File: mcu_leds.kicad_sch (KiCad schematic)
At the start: 8 parts, among them U1201 SN74LVC1G07DCKR

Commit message: Finish transitioning to RP2040
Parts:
- renumbered C1202 to C3901, D1203 to D3901, D1204 to D3902, D1205 to D3903, R1203 to R3901, R1206 to R3902, R1209 to R3903, U1201 to U3901
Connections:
- net VCC is gone; now on net +3.3V: R3903.1
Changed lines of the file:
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@@
 		)
 	)
-	(hierarchical_label "VCC"
-		(shape input)
-		(at 168.91 80.01 90)
-		(effects
-			(font
-				(size 1.27 1.27)
-			)
-			(justify left)
+	(symbol
+		(lib_id "power:+3.3V")
+		(at 168.91 80.01 0)
+		(unit 1)
+		(exclude_from_sim no)
+		(in_bom yes)
+		(on_board yes)
+		(dnp no)
+		(fields_autoplaced yes)
+		(property "Reference" "#PWR03907"
+			(at 168.91 83.82 0)
+			(effects
+				(font
+					(size 1.27 1.27)
+				)
+				(hide yes)
+			)
+		)
+		(property "Value" "+3.3V"
+			(at 171.45 78.7399 0)
+			(effects
+				(font
+					(size 1.27 1.27)
+				)
+				(justify left)
+			)
+		)
+		(property "Footprint" ""
+			(at 168.91 80.01 0)
+			(effects
+				(font
+					(size 1.27 1.27)
+				)
+				(hide yes)
+			)
+		)
+		(property "Datasheet" ""
+			(at 168.91 80.01 0)
+			(effects
+				(font
+					(size 1.27 1.27)
+				)
+				(hide yes)
+			)
+		)
+		(property "Description" "Power symbol creates a global label with name \"+3.3V\""
+			(at 168.91 80.01 0)
+			(effects
+				(font
+					(size 1.27 1.27)
+				)
+				(hide yes)
+			)
+		)
+		(pin "1"
+		)
+		(instances
+			(project "HALPI2"
+				(path "/abc482bd-3f17-4d35-80db-1da3dcdb5c27/850df4bf-e40a-4082-adc2-76804638b949/91cc707d-e26c-4ece-92aa-858b9215776e"
+					(reference "#PWR03907")
+					(unit 1)
+				)
+			)
 		)
 	)
@@
 		(on_board yes)
 		(dnp no)
-		(property "Reference" "R1209"
+		(property "Reference" "R3903"
 			(at 170.688 82.6516 0)
 			(effects
@@
 			(project "HALPI2"
 				(path "/abc482bd-3f17-4d35-80db-1da3dcdb5c27/850df4bf-e40a-4082-adc2-76804638b949/91cc707d-e26c-4ece-92aa-858b9215776e"
-					(reference "R1209")
+					(reference "R3903")
 					(unit 1)
 				)
@@
 		(dnp no)
 		(fields_autoplaced yes)
-		(property "Reference" "D1204"
+		(property "Reference" "D3902"
 			(at 156.21 91.7574 90)
 			(effects
@@
 			(project "HALPI2"
 				(path "/abc482bd-3f17-4d35-80db-1da3dcdb5c27/850df4bf-e40a-4082-adc2-76804638b949/91cc707d-e26c-4ece-92aa-858b9215776e"
-					(reference "D1204")
+					(reference "D3902")
 					(unit 1)
 				)
@@
 		(on_board yes)
 		(dnp no)
-		(property "Reference" "#PWR03817"
+		(property "Reference" "#PWR03901"
 			(at 106.68 90.17 0)
 			(effects
@@
 			(project "HALPI2"
 				(path "/abc482bd-3f17-4d35-80db-1da3dcdb5c27/850df4bf-e40a-4082-adc2-76804638b949/91cc707d-e26c-4ece-92aa-858b9215776e"
-					(reference "#PWR03817")
+					(reference "#PWR03901")
 					(unit 1)
 				)
@@
 		(on_board yes)
 		(dnp no)
-		(property "Reference" "D1205"
+		(property "Reference" "D3903"
 			(at 171.9072 90.4494 90)
 			(effects
@@
 			(project "HALPI2"
 				(path "/abc482bd-3f17-4d35-80db-1da3dcdb5c27/850df4bf-e40a-4082-adc2-76804638b949/91cc707d-e26c-4ece-92aa-858b9215776e"
-					(reference "D1205")
+					(reference "D3903")
 					(unit 1)
 				)
@@
 		(on_board yes)
 		(dnp no)
-		(property "Reference" "D1203"
+		(property "Reference" "D3901"
 			(at 141.4272 90.4494 90)
 			(effects
@@
 			(project "HALPI2"
 				(path "/abc482bd-3f17-4d35-80db-1da3dcdb5c27/850df4bf-e40a-4082-adc2-76804638b949/91cc707d-e26c-4ece-92aa-858b9215776e"
-					(reference "D1203")
+					(reference "D3901")
 					(unit 1)
 				)
@@
 		(dnp no)
 		(fields_autoplaced yes)
-		(property "Reference" "#PWR03820"
+		(property "Reference" "#PWR03904"
 			(at 138.43 83.82 0)
 			(effects
@@
 			(project "HALPI2"
 				(path "/abc482bd-3f17-4d35-80db-1da3dcdb5c27/850df4bf-e40a-4082-adc2-76804638b949/91cc707d-e26c-4ece-92aa-858b9215776e"
-					(reference "#PWR03820")
+					(reference "#PWR03904")
 					(unit 1)
 				)
@@
 		(on_board yes)
 		(dnp no)
-		(property "Reference" "U1201"
+		(property "Reference" "U3901"
 			(at 131.064 98.806 0)
 			(effects
@@
 			(project "HALPI2"
 				(path "/abc482bd-3f17-4d35-80db-1da3dcdb5c27/850df4bf-e40a-4082-adc2-76804638b949/91cc707d-e26c-4ece-92aa-858b9215776e"
-					(reference "U1201")
+					(reference "U3901")
 					(unit 1)
 				)
@@
 		(dnp no)
 		(fields_autoplaced yes)
-		(property "Reference" "#PWR03818"
+		(property "Reference" "#PWR03902"
 			(at 119.38 83.82 0)
 			(effects
@@
 			(project "HALPI2"
 				(path "/abc482bd-3f17-4d35-80db-1da3dcdb5c27/850df4bf-e40a-4082-adc2-76804638b949/91cc707d-e26c-4ece-92aa-858b9215776e"
-					(reference "#PWR03818")
+					(reference "#PWR03902")
 					(unit 1)
 				)
@@
 		(on_board yes)
 		(dnp no)
-		(property "Reference" "R1203"
+		(property "Reference" "R3901"
 			(at 140.208 82.6516 0)
 			(effects
@@
 			(project "HALPI2"
 				(path "/abc482bd-3f17-4d35-80db-1da3dcdb5c27/850df4bf-e40a-4082-adc2-76804638b949/91cc707d-e26c-4ece-92aa-858b9215776e"
-					(reference "R1203")
+					(reference "R3901")
 					(unit 1)
 				)
@@
 		(dnp no)
 		(fields_autoplaced yes)
-		(property "Reference" "#PWR03821"
+		(property "Reference" "#PWR03905"
 			(at 152.4 83.82 0)
 			(effects
@@
 			(project "HALPI2"
 				(path "/abc482bd-3f17-4d35-80db-1da3dcdb5c27/850df4bf-e40a-4082-adc2-76804638b949/91cc707d-e26c-4ece-92aa-858b9215776e"
-					(reference "#PWR03821")
+					(reference "#PWR03905")
 					(unit 1)
 				)
@@
 		(on_board yes)
 		(dnp no)
-		(property "Reference" "R1206"
+		(property "Reference" "R3902"
 			(at 154.178 82.6516 0)
 			(effects
@@
 			(project "HALPI2"
 				(path "/abc482bd-3f17-4d35-80db-1da3dcdb5c27/850df4bf-e40a-4082-adc2-76804638b949/91cc707d-e26c-4ece-92aa-858b9215776e"
-					(reference "R1206")
+					(reference "R3902")
 					(unit 1)
 				)
@@
 		(dnp no)
 		(fields_autoplaced yes)
-		(property "Reference" "C1202"
+		(property "Reference" "C3901"
 			(at 113.03 76.2 90)
 			(effects
@@
 			(project "HALPI2"
 				(path "/abc482bd-3f17-4d35-80db-1da3dcdb5c27/850df4bf-e40a-4082-adc2-76804638b949/91cc707d-e26c-4ece-92aa-858b9215776e"
-					(reference "C1202")
+					(reference "C3901")
 					(unit 1)
 				)
@@
 		(on_board yes)
 		(dnp no)
-		(property "Reference" "#PWR03822"
+		(property "Reference" "#PWR03906"
 			(at 168.91 104.14 0)
 			(effects
@@
 			(project "HALPI2"
 				(path "/abc482bd-3f17-4d35-80db-1da3dcdb5c27/850df4bf-e40a-4082-adc2-76804638b949/91cc707d-e26c-4ece-92aa-858b9215776e"
-					(reference "#PWR03822")
+					(reference "#PWR03906")
 					(unit 1)
 				)
@@
 		(on_board yes)
 		(dnp no)
-		(property "Reference" "#PWR03819"
+		(property "Reference" "#PWR03903"
 			(at 119.38 111.76 0)
 			(effects
@@
 			(project "HALPI2"
 				(path "/abc482bd-3f17-4d35-80db-1da3dcdb5c27/850df4bf-e40a-4082-adc2-76804638b949/91cc707d-e26c-4ece-92aa-858b9215776e"
-					(reference "#PWR03819")
-					(unit 1)
-				)
+					(reference "#PWR03903")
+					(unit 1)
+				)

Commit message: Apply part PCBA position corrections
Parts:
- U3901: JLCPCB_CORRECTION (none) -> 0;0;180
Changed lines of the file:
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@@
+			)
+		)
+		(property "JLCPCB_CORRECTION" "0;0;180"
+			(at 124.46 95.25 0)
+			(effects
+				(font
+					(size 1.27 1.27)
+				)
+				(hide yes)
 			)
 		)

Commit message: Reannotate the board
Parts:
- added R131: 100k, Resistor_SMD:R_0402_1005Metric, symbol Device:R
- renumbered C3901 to C184, D3901 to D40, D3902 to D41, D3903 to D42, R3901 to R132, R3902 to R133, R3903 to R134, U3901 to U55
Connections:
- net +3.3V: now also R131.1
- net ~{LED_PWR}: now also R131.2

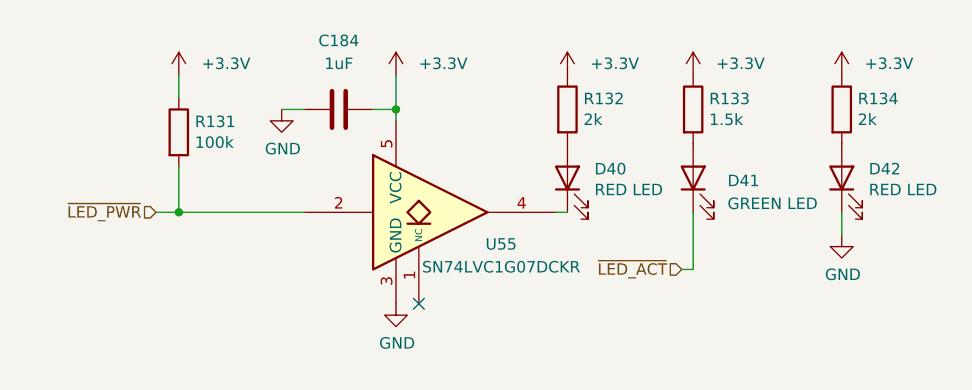
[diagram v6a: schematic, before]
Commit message: Add GND/3.3V/5V headers, add missing JLC part numbers
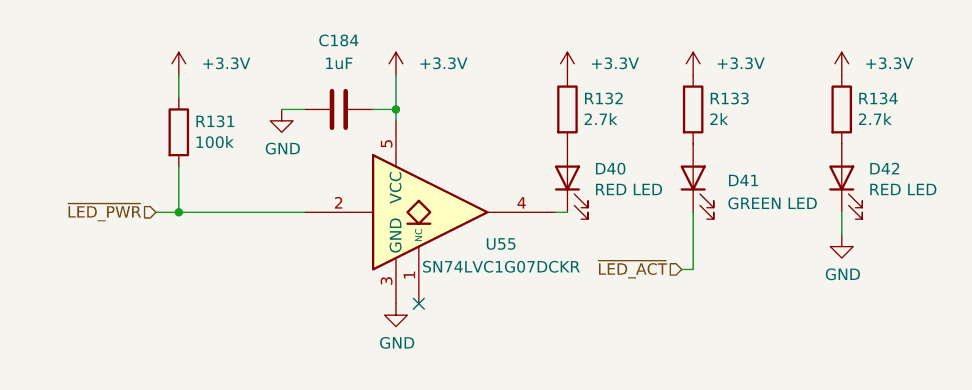
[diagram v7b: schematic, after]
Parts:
- R131: LCSC (none) -> C25741
- R132, R134: value 2k -> 2.7k; footprint Resistor_SMD:R_0402_1005Metric -> Resistor_SMD:R_0603_1608Metric; LCSC C4109 -> C13167
- R133: value 1.5k -> 2k; LCSC C25867 -> C4109
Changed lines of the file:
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@@
 			)
 		)
-		(property "Value" "2k"
+		(property "Value" "2.7k"
 			(at 170.688 84.963 0)
 			(effects
@@
 			)
 		)
-		(property "Footprint" "Resistor_SMD:R_0402_1005Metric"
+		(property "Footprint" "Resistor_SMD:R_0603_1608Metric"
 			(at 167.132 83.82 90)
 			(effects
@@
 			)
 		)
-		(property "LCSC" "C4109"
+		(property "LCSC" "C13167"
 			(at 168.91 83.82 0)
 			(effects
@@
 			)
 		)
-		(property "Value" "2k"
+		(property "Value" "2.7k"
 			(at 140.208 84.963 0)
 			(effects
@@
 			)
 		)
-		(property "Footprint" "Resistor_SMD:R_0402_1005Metric"
+		(property "Footprint" "Resistor_SMD:R_0603_1608Metric"
 			(at 136.652 83.82 90)
 			(effects
@@
 			)
 		)
-		(property "LCSC" "C4109"
+		(property "LCSC" "C13167"
 			(at 138.43 83.82 0)
 			(effects
@@
 			)
 		)
-		(property "LCSC" ""
+		(property "LCSC" "C25741"
 			(at 95.25 86.36 0)
 			(effects
@@
 			)
 		)
-		(property "Value" "1.5k"
+		(property "Value" "2k"
 			(at 154.178 84.963 0)
 			(effects
@@
 			)
 		)
-		(property "LCSC" "C25867"
+		(property "LCSC" "C4109"
 			(at 152.4 83.82 0)
 			(effects

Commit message: FInal v0.2.0 proto changes
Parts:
- renumbered C184 to C187
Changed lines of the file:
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@@
 		(dnp no)
 		(fields_autoplaced yes)
-		(property "Reference" "#PWR0351"
+		(property "Reference" "#PWR0371"
 			(at 168.91 83.82 0)
 			(effects
@@
 			(project "HALPI2"
 				(path "/abc482bd-3f17-4d35-80db-1da3dcdb5c27/850df4bf-e40a-4082-adc2-76804638b949/91cc707d-e26c-4ece-92aa-858b9215776e"
-					(reference "#PWR0351")
+					(reference "#PWR0371")
 					(unit 1)
 				)
@@
 		(dnp no)
 		(fields_autoplaced yes)
-		(property "Reference" "#PWR0345"
+		(property "Reference" "#PWR0365"
 			(at 95.25 83.82 0)
 			(effects
@@
 			(project "HALPI2"
 				(path "/abc482bd-3f17-4d35-80db-1da3dcdb5c27/850df4bf-e40a-4082-adc2-76804638b949/91cc707d-e26c-4ece-92aa-858b9215776e"
-					(reference "#PWR0345")
+					(reference "#PWR0365")
 					(unit 1)
 				)
@@
 		(on_board yes)
 		(dnp no)
-		(property "Reference" "#PWR0346"
+		(property "Reference" "#PWR0366"
 			(at 106.68 90.17 0)
 			(effects
@@
 			(project "HALPI2"
 				(path "/abc482bd-3f17-4d35-80db-1da3dcdb5c27/850df4bf-e40a-4082-adc2-76804638b949/91cc707d-e26c-4ece-92aa-858b9215776e"
-					(reference "#PWR0346")
+					(reference "#PWR0366")
 					(unit 1)
 				)
@@
 		(dnp no)
 		(fields_autoplaced yes)
-		(property "Reference" "#PWR0349"
+		(property "Reference" "#PWR0369"
 			(at 138.43 83.82 0)
 			(effects
@@
 			(project "HALPI2"
 				(path "/abc482bd-3f17-4d35-80db-1da3dcdb5c27/850df4bf-e40a-4082-adc2-76804638b949/91cc707d-e26c-4ece-92aa-858b9215776e"
-					(reference "#PWR0349")
+					(reference "#PWR0369")
 					(unit 1)
 				)
@@
 		(dnp no)
 		(fields_autoplaced yes)
-		(property "Reference" "#PWR0347"
+		(property "Reference" "#PWR0367"
 			(at 119.38 83.82 0)
 			(effects
@@
 			(project "HALPI2"
 				(path "/abc482bd-3f17-4d35-80db-1da3dcdb5c27/850df4bf-e40a-4082-adc2-76804638b949/91cc707d-e26c-4ece-92aa-858b9215776e"
-					(reference "#PWR0347")
+					(reference "#PWR0367")
 					(unit 1)
 				)
@@
 		(dnp no)
 		(fields_autoplaced yes)
-		(property "Reference" "#PWR0350"
+		(property "Reference" "#PWR0370"
 			(at 152.4 83.82 0)
 			(effects
@@
 			(project "HALPI2"
 				(path "/abc482bd-3f17-4d35-80db-1da3dcdb5c27/850df4bf-e40a-4082-adc2-76804638b949/91cc707d-e26c-4ece-92aa-858b9215776e"
-					(reference "#PWR0350")
+					(reference "#PWR0370")
 					(unit 1)
 				)
@@
 		(dnp no)
 		(fields_autoplaced yes)
-		(property "Reference" "C184"
+		(property "Reference" "C187"
 			(at 113.03 76.2 90)
 			(effects
@@
 			(project "HALPI2"
 				(path "/abc482bd-3f17-4d35-80db-1da3dcdb5c27/850df4bf-e40a-4082-adc2-76804638b949/91cc707d-e26c-4ece-92aa-858b9215776e"
-					(reference "C184")
+					(reference "C187")
 					(unit 1)
 				)
@@
 		(on_board yes)
 		(dnp no)
-		(property "Reference" "#PWR0352"
+		(property "Reference" "#PWR0372"
 			(at 168.91 104.14 0)
 			(effects
@@
 			(project "HALPI2"
 				(path "/abc482bd-3f17-4d35-80db-1da3dcdb5c27/850df4bf-e40a-4082-adc2-76804638b949/91cc707d-e26c-4ece-92aa-858b9215776e"
-					(reference "#PWR0352")
+					(reference "#PWR0372")
 					(unit 1)
 				)
@@
 		(on_board yes)
 		(dnp no)
-		(property "Reference" "#PWR0348"
+		(property "Reference" "#PWR0368"
 			(at 119.38 111.76 0)
 			(effects
@@
 			(project "HALPI2"
 				(path "/abc482bd-3f17-4d35-80db-1da3dcdb5c27/850df4bf-e40a-4082-adc2-76804638b949/91cc707d-e26c-4ece-92aa-858b9215776e"
-					(reference "#PWR0348")
-					(unit 1)
-				)
+					(reference "#PWR0368")
+					(unit 1)
+				)
